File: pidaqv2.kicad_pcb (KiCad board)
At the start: 2 copper layers, 66 x 66 mm, 20 parts, among them J1 Raspberry_Pi_2_3, U1 INA2126E_250, U2 ADS114S08BIPBS, U3 ADS114S08BIPBS

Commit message: ads1261
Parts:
- removed C1, C4, C7, C8, C9: 0.1uF, Capacitor_SMD:C_0805_2012Metric_Pad1.15x1.40mm_HandSolder
- removed C2, C5: 330nF, Capacitor_SMD:C_0805_2012Metric_Pad1.15x1.40mm_HandSolder
- removed C3, C6: 1uF, Capacitor_SMD:C_0805_2012Metric_Pad1.15x1.40mm_HandSolder
- removed J1: Raspberry_Pi_2_3, Connector_PinHeader_2.54mm:PinHeader_2x20_P2.54mm_Vertical
- removed JAIN0: Screw_Terminal_01x10, TerminalBlock_TE-Connectivity:TerminalBlock_TE_1-282834-0_1x10_P2.54mm_Horizontal
- removed JAIN1: Screw_Terminal_01x12, TerminalBlock_TE-Connectivity:TerminalBlock_TE_1-282834-2_1x12_P2.54mm_Horizontal
- removed JLC1, JTC-1: Screw_Terminal_01x06, TerminalBlock_TE-Connectivity:TerminalBlock_TE_282834-6_1x06_P2.54mm_Horizontal
- removed MK1, MK2, MK3: MountingHole_Pad, MountingHole:MountingHole_2.7mm_M2.5_ISO14580_Pad
- removed U1: INA2126E_250, footprints:INA2126E&slash_250
- removed U2, U3: ADS114S08BIPBS, footprints:ADS114S08BIPBS
- added C101: 0.1uF, Capacitor_SMD:C_0603_1608Metric, F.Cu at (124.6, 97.3)
- added C102: 0.1uF, Capacitor_SMD:C_0603_1608Metric, F.Cu at (127.8, 96.3)
- added C201: 4.7nF C0G, Capacitor_SMD:C_0603_1608Metric, F.Cu at (137.3, 91.5)
- added C202: 1uF, Capacitor_SMD:C_0603_1608Metric, F.Cu at (134.6, 93.6)
- added C203: 10uF, Capacitor_SMD:C_0603_1608Metric, F.Cu at (135.4, 95.9)
- added C204: 1uF, Capacitor_SMD:C_0603_1608Metric, F.Cu at (148.3, 95.5)
- added C205: 1uF, Capacitor_SMD:C_0603_1608Metric, F.Cu at (145.1, 97.7)
- added C206: 10uF, Capacitor_SMD:C_0603_1608Metric, F.Cu at (134.6, 91.3)
- added C301: 4.7nF C0G, Capacitor_SMD:C_0603_1608Metric, F.Cu at (140.3, 119.9)
- added C302: 1uF, Capacitor_SMD:C_0603_1608Metric, F.Cu at (140.9, 117.0)
- added C303: 10uF, Capacitor_SMD:C_0603_1608Metric, F.Cu at (140.9, 115.1)
- added C304: 1uF, Capacitor_SMD:C_0603_1608Metric, F.Cu at (129.5, 114.0)
- added C305: 1uF, Capacitor_SMD:C_0603_1608Metric, F.Cu at (132.5, 111.6)
- added C306: 10uF, Capacitor_SMD:C_0603_1608Metric, F.Cu at (143.6, 118.9)
- added H101: MountingHole, MountingHole:MountingHole_3.2mm_M3_ISO7380, F.Cu at (172.7, 134.6)
- added H102: MountingHole, MountingHole:MountingHole_3.2mm_M3_ISO7380, F.Cu at (101.6, 134.6)
- added H103: MountingHole, MountingHole:MountingHole_3.2mm_M3_ISO7380, F.Cu at (172.7, 73.7)
- added H104: MountingHole, MountingHole:MountingHole_3.2mm_M3_ISO7380, F.Cu at (101.6, 73.7)
- added J101: Conn_02x04_Odd_Even, Connector_PinHeader_2.54mm:PinHeader_2x04_P2.54mm_Vertical, F.Cu at (165.1, 94.0)
- added J102: Conn_01x03, Connector_PinHeader_2.54mm:PinHeader_1x03_P2.54mm_Vertical, F.Cu at (162.6, 114.3)
- added J103: Screw_Terminal_01x10, TerminalBlock_Phoenix:TerminalBlock_Phoenix_MKDS-1,5-10-5.08_1x10_P5.08mm_Horizontal, F.Cu at (116.8, 81.3)
- added J104: Screw_Terminal_01x08, TerminalBlock_Phoenix:TerminalBlock_Phoenix_MPT-0,5-8-2.54_1x08_P2.54mm_Horizontal, F.Cu at (111.8, 129.5)
- added J105: Screw_Terminal_01x06, TerminalBlock_Phoenix:TerminalBlock_Phoenix_MKDS-3-6-5.08_1x06_P5.08mm_Horizontal, F.Cu at (111.8, 118.6)
- added J106: Screw_Terminal_01x08, TerminalBlock_Phoenix:TerminalBlock_Phoenix_MPT-0,5-8-2.54_1x08_P2.54mm_Horizontal, F.Cu at (134.6, 129.5)
- added J107: Conn_01x01_Female, Connector_PinHeader_2.54mm:PinHeader_1x01_P2.54mm_Vertical, F.Cu at (129.7, 88.8)
- added U101: INA2126E_250, footprints:INA2126E&slash_250, F.Cu at (124.8, 103.4)
- added U201: ADS1261BIRHBR, footprints:ADS1261BIRHBR, F.Cu at (142.0, 93.8)
- added U301: ADS1261BIRHBR, footprints:ADS1261BIRHBR, F.Cu at (134.6, 116.8)
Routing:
- net +3V3: track 56.3 -> 145.3 mm, vias 2 -> 3
- net TC-: track 0.00 -> 76.7 mm
- net +2.5V: track 51.8 -> 0.00 mm, vias 2 -> 0
- net /ADC_Module/A11: track 39.3 -> 0.00 mm
- net /sheet5F3BC562/A1: track 38.4 -> 0.00 mm
- net ~CS1: track 0.00 -> 37.6 mm
- net /ADC_Module/A10: track 37.1 -> 0.00 mm
- net /sheet5F3BC562/A0: track 35.6 -> 0.00 mm
- net /ADC_Module/A9: track 34.9 -> 0.00 mm
- net /ADC_Module/A8: track 32.8 -> 0.00 mm
- net /sheet5F3BC562/A2: track 32.1 -> 0.00 mm
- net /sheet5F3BC562/A5: track 31.5 -> 0.00 mm
- net /sheet5F3BC562/A4: track 31.3 -> 0.00 mm
- net /sheet5F3BC562/A3: track 31.1 -> 0.00 mm
- net /ADC0/AIN0: track 0.00 -> 30.0 mm
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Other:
- board size 66 x 66 mm -> 81.3 x 71.1 mm
- net class Default: clearance 0.1778 -> 0.2032; trace_width 0.1778 -> 0.2032
- rule pad_to_mask_clearance: 0.051 -> 0
- rule trace_clearance: 0.1778 -> 0.2032
- rule trace_min: 0.1778 -> 0.2032
- rule via_min_drill: 0.3 -> 0.381
- rule via_min_size: 0.3048 -> 0.3302
- board text added: "+3.3V"
- board text added: "+5V"
- board text added: "+EXC"
- board text added: "LC0+"
- board text added: "LC0-"
- board text added: "LC1+"
- board text added: "LC1-"
- board text added: "MISO"
- board text added: "MOSI"
- board text added: "PT0"
- board text added: "PT1"
- board text added: "PT2"
- board text added: "PT3"
- board text added: "PT4"
- board text added: "PT5"
- board text added: "PT6"
- board text added: "PT7"
- board text added: "PT8"
- board text added: "PT9"
- board text added: "Raspi mounted here"
- board text added: "SCLK"
- board text added: "TC0+"
- board text added: "TC0-"
- board text added: "TC1+"
- board text added: "TC1-"
- board text added: "TC2+"
- board text added: "TC2-"
- board text added: "TC3+"
- board text added: "TC3-"
- board text added: "TC4+"
- board text added: "TC4-"
- board text added: "TC5+"
- board text added: "TC5-"
- board text added: "TC6+"
- board text added: "TC6-"
- board text added: "TC7+"
- board text added: "TC7-"
- board text added: "UCLA Rocket Project DAQ 2020-2021"
- board text added: "~CS0"
- board text added: "~CS1"
- board text removed: "0"
- board text removed: "0+"
- board text removed: "0-"
- board text removed: "1"
- board text removed: "1+"
- board text removed: "1-"
- board text removed: "10"
- board text removed: "11"
- board text removed: "2"
- board text removed: "3"
- board text removed: "4"
- board text removed: "5"
- board text removed: "6"
- board text removed: "7"
- board text removed: "8"
- board text removed: "9"
- board text removed: "EXC"
- board text removed: "Load Cells"
- board text removed: "Thermocouple -'s"
- board text removed: "UCLA Rocket Project DAQ Module V1"
- board text removed: "V=2.5V"

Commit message: last highfreq
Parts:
- J107: value Conn_01x01_Female -> Conn_01x03_Male; footprint Connector_PinHeader_2.54mm:PinHeader_1x01_P2.54mm_Vertical -> Connector_PinHeader_2.54mm:PinHeader_1x03_P2.54mm_Vertical
- moved J107 20.1 mm to (109.7, 86.4), turned to 180 degrees
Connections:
- J104 pad 1: TC7 -> (no net)
- J107 pad 1: /ADC0/AIN- -> 2.5V
- U301 pad 25: TC7 -> (no net)
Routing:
- net 2.5V: track 25.1 -> 53.5 mm, vias 2 -> 3
- net TC7: track 27.2 -> 0.00 mm
- net (no net): track 0.00 -> 27.2 mm
- net /ADC0/AIN-: track 11.5 -> 34.2 mm
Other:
- net class Power added: clearance 0.2032, trace_width 0.508, via_dia 0.8, via_drill 0.4
- board text added: "2.5V"
- board text added: "AIN-"

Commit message: boi did i cut up that ground plane
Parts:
- removed C101, C102: 0.1uF, Capacitor_SMD:C_0603_1608Metric
- removed J106: Screw_Terminal_01x08, TerminalBlock_Phoenix:TerminalBlock_Phoenix_MPT-0,5-8-2.54_1x08_P2.54mm_Horizontal
- removed J107: Conn_01x03_Male, Connector_PinHeader_2.54mm:PinHeader_1x03_P2.54mm_Vertical
- removed U101: INA2126E_250, footprints:INA2126E&slash_250
- added A101: Arduino_UNO_R3, Module:Arduino_UNO_R3, F.Cu at (86.4, 71.1)
- added C401: 0.1uF, Capacitor_SMD:C_0805_2012Metric_Pad1.15x1.40mm_HandSolder, F.Cu at (120.2, 98.5)
- added C402: 10uF, Capacitor_SMD:C_0805_2012Metric_Pad1.15x1.40mm_HandSolder, F.Cu at (123.2, 98.5)
- added R201: 4.7K, Resistor_SMD:R_0805_2012Metric_Pad1.15x1.40mm_HandSolder, F.Cu at (81.6, 101.4)
- added R301: 4.7K, Resistor_SMD:R_0805_2012Metric_Pad1.15x1.40mm_HandSolder, F.Cu at (102.9, 85.4)
- added U401: AD8426ACPZ-R7, footprints:AD8426ACPZ-R7, F.Cu at (119.7, 93.2)
- C201, C202, C203, C204, C205, C206, C301, C302, C303, C304, C305, C306: footprint Capacitor_SMD:C_0603_1608Metric -> Capacitor_SMD:C_0805_2012Metric_Pad1.15x1.40mm_HandSolder
- J101: value Conn_02x04_Odd_Even -> Screw_Terminal_01x11; footprint Connector_PinHeader_2.54mm:PinHeader_2x04_P2.54mm_Vertical -> TerminalBlock_Phoenix:TerminalBlock_Phoenix_MKDS-3-11-5.08_1x11_P5.08mm_Horizontal
- J102: value Conn_01x03 -> Screw_Terminal_01x06; footprint Connector_PinHeader_2.54mm:PinHeader_1x03_P2.54mm_Vertical -> TerminalBlock_Phoenix:TerminalBlock_Phoenix_MKDS-1,5-6-5.08_1x06_P5.08mm_Horizontal
- J103: value Screw_Terminal_01x10 -> Conn_01x02_Male; footprint TerminalBlock_Phoenix:TerminalBlock_Phoenix_MKDS-1,5-10-5.08_1x10_P5.08mm_Horizontal -> Connector_PinHeader_2.54mm:PinHeader_1x02_P2.54mm_Vertical
- J105: value Screw_Terminal_01x06 -> Screw_Terminal_01x04; footprint TerminalBlock_Phoenix:TerminalBlock_Phoenix_MKDS-3-6-5.08_1x06_P5.08mm_Horizontal -> TerminalBlock_Phoenix:TerminalBlock_Phoenix_MPT-0,5-4-2.54_1x04_P2.54mm_Horizontal
- U201, U301: footprint footprints:ADS1261BIRHBR -> Package_DFN_QFN:Texas_S-PVQFN-N32_EP3.45x3.45mm
- moved H103 112.8 mm to (61.0, 58.4)
- moved H101 111.7 mm to (61.3, 143.1)
- moved J101 104.0 mm to (69.5, 134.9)
- moved H102 85.2 mm to (139.7, 58.4)
- moved H104 79.2 mm to (139.7, 143.1)
- moved C204 77.6 mm to (71.5, 105.7), turned to 180 degrees
- moved C205 69.5 mm to (75.7, 101.9), turned to 180 degrees
- moved J104 66.1 mm to (114.3, 63.5), turned to 180 degrees
- moved U201 65.2 mm to (78.2, 107.4), turned to 180 degrees
- moved C301 58.7 mm to (99.9, 77.3), turned to 270 degrees
- moved C306 58.4 mm to (96.3, 84.7), turned to 180 degrees
- moved J103 58.2 mm to (78.7, 125.2), turned to 90 degrees
- moved C302 57.2 mm to (96.3, 81.1), turned to 180 degrees
- moved C201 55.8 mm to (84.5, 109.8), turned to 90 degrees
- moved J105 52.7 mm to (134.6, 71.1), turned to 270 degrees
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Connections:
- net TC- renamed /ADC1/AINCOM
- C203 pad 1: 2.5V -> /ADC0/REF2.5V
- J101 pad 1: GND -> /ADC0/AIN9
- J101 pad 2: MOSI -> /ADC0/AIN8
- J101 pad 3: (no net) -> /ADC0/AIN7
- J101 pad 4: MISO -> /ADC0/AIN6
- J101 pad 5: ~CS0 -> /ADC0/AIN5
- J101 pad 6: SCLK -> /ADC0/AIN4
- J101 pad 7: ~CS1 -> /ADC0/AIN3
- J101 pad 8: GND -> /ADC0/AIN2
- J102 pad 1: +5V -> /amplifier/A+
- J102 pad 2: +3V3 -> /amplifier/A-
- J102 pad 3: GND -> /amplifier/B+
- J103 pad 1: /ADC0/AIN0 -> /ADC0/AINCOM
- J103 pad 2: /ADC0/AIN1 -> GND
- J104 pad 1: (no net) -> /ADC1/AIN3
- J104 pad 3: TC6 -> /ADC1/AIN2
- J104 pad 5: TC5 -> /ADC1/AIN1
- J104 pad 7: TC4 -> /ADC1/AIN0
- J105 pad 1: GND -> /ADC1/AIN4
- J105 pad 2: LC0- -> /ADC1/AIN5
- J105 pad 3: LC0+ -> /ADC1/AIN6
- J105 pad 4: LC1- -> /ADC1/AIN7
- U201 pad 1: /ADC0/AIN- -> /ADC0/AINCOM
- U201 pad 6: 2.5V -> /ADC0/REF2.5V
- U301 pad 23: LC1 -> /A
- U301 pad 24: LC0 -> /B
- U301 pad 25: (no net) -> /ADC1/AIN7
- U301 pad 26: TC6 -> /ADC1/AIN6
- U301 pad 27: TC5 -> /ADC1/AIN5
- U301 pad 28: TC4 -> /ADC1/AIN4
- U301 pad 29: TC3 -> /ADC1/AIN3
- U301 pad 30: TC2 -> /ADC1/AIN2
- U301 pad 31: TC1 -> /ADC1/AIN1
- U301 pad 32: TC0 -> /ADC1/AIN0
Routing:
- net /ADC0/REF2.5V: track 0.00 -> 64.6 mm, vias 0 -> 2
- net 2.5V: track 53.5 -> 0.00 mm, vias 3 -> 0
- net /amplifier/A-: track 0.00 -> 50.0 mm
- net /ADC1/REF2.5V: track 3.49 -> 45.2 mm, vias 0 -> 4
- net /ADC0/AIN1: track 24.7 -> 61.5 mm
- net /ADC0/AIN2: track 20.2 -> 56.8 mm
- net /ADC0/AIN0: track 30.0 -> 66.5 mm
- net /ADC0/AIN3: track 15.7 -> 52.1 mm
- net /ADC1/AINCOM: track 76.7 -> 41.1 mm
- net /ADC0/AIN4: track 12.9 -> 47.9 mm
- net /ADC0/AIN-: track 34.2 -> 0.00 mm
- net /ADC1/AIN4: track 0.00 -> 32.7 mm
- net /ADC0/AIN5: track 10.4 -> 42.8 mm
- net /ADC1/AIN6: track 0.00 -> 31.7 mm
- net /ADC1/AIN5: track 0.00 -> 31.2 mm
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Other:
- board size 81.3 x 71.1 mm -> 86.4 x 92.1 mm
- net class Default: clearance 0.2032 -> 0.1778; trace_width 0.2032 -> 0.1778
- rule trace_clearance: 0.2032 -> 0.1778
- rule trace_min: 0.2032 -> 0.1524
- board text removed: "+3.3V"
- board text removed: "+5V"
- board text removed: "+EXC"
- board text removed: "2.5V"
- board text removed: "AIN-"
- board text removed: "GND"
- board text removed: "LC0+"
- board text removed: "LC0-"
- board text removed: "LC1+"
- board text removed: "LC1-"
- board text removed: "MISO"
- board text removed: "MOSI"
- board text removed: "PT0"
- board text removed: "PT1"
- board text removed: "PT2"
- board text removed: "PT3"
- board text removed: "PT4"
- board text removed: "PT5"
- board text removed: "PT6"
- board text removed: "PT7"
- board text removed: "PT8"
- board text removed: "PT9"
- board text removed: "Raspi mounted here"
- board text removed: "SCLK"
- board text removed: "TC0+"
- board text removed: "TC0-"
- board text removed: "TC1+"
- board text removed: "TC1-"
- board text removed: "TC2+"
- board text removed: "TC2-"
- board text removed: "TC3+"
- board text removed: "TC3-"
- board text removed: "TC4+"
- board text removed: "TC4-"
- board text removed: "TC5+"
- board text removed: "TC5-"
- board text removed: "TC6+"
- board text removed: "TC6-"
- board text removed: "TC7+"
- board text removed: "TC7-"
- board text removed: "UCLA Rocket Project DAQ 2020-2021"
- board text removed: "~CS0"
- board text removed: "~CS1"

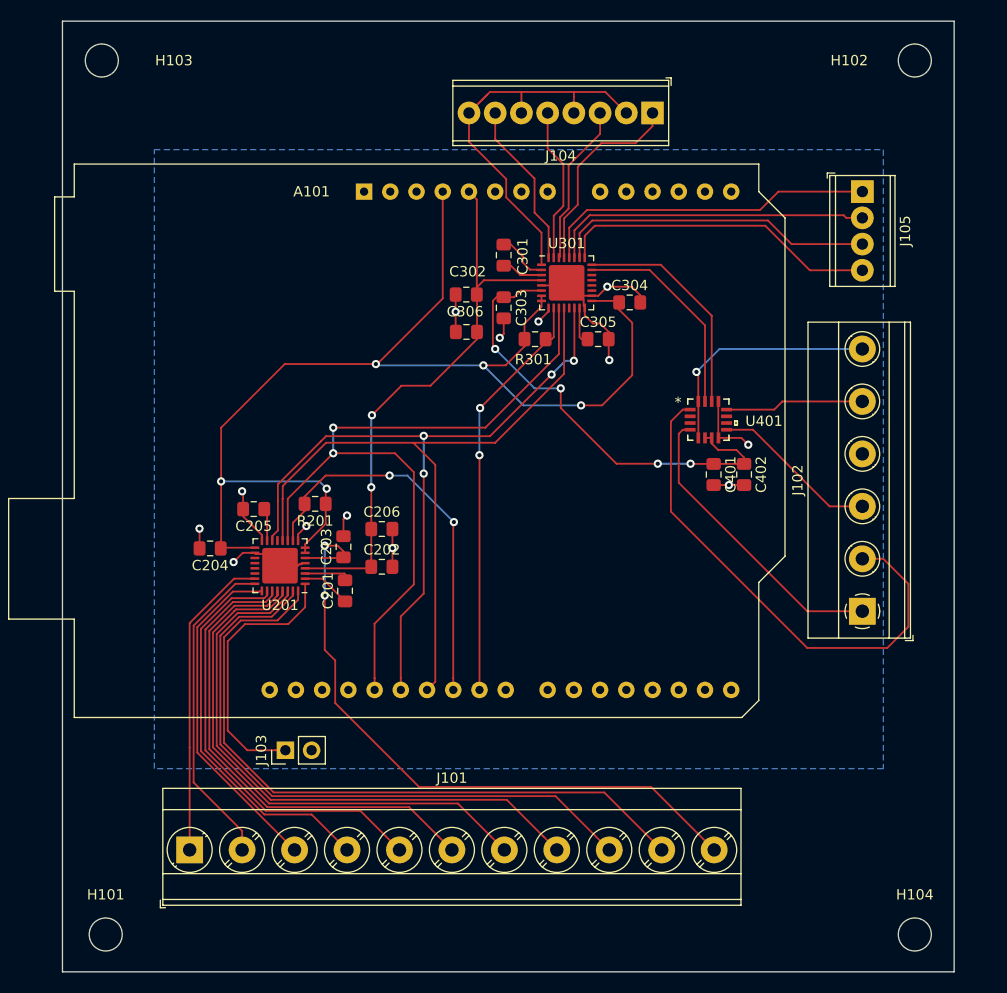
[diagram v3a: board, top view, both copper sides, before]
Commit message: add silkscreen labels
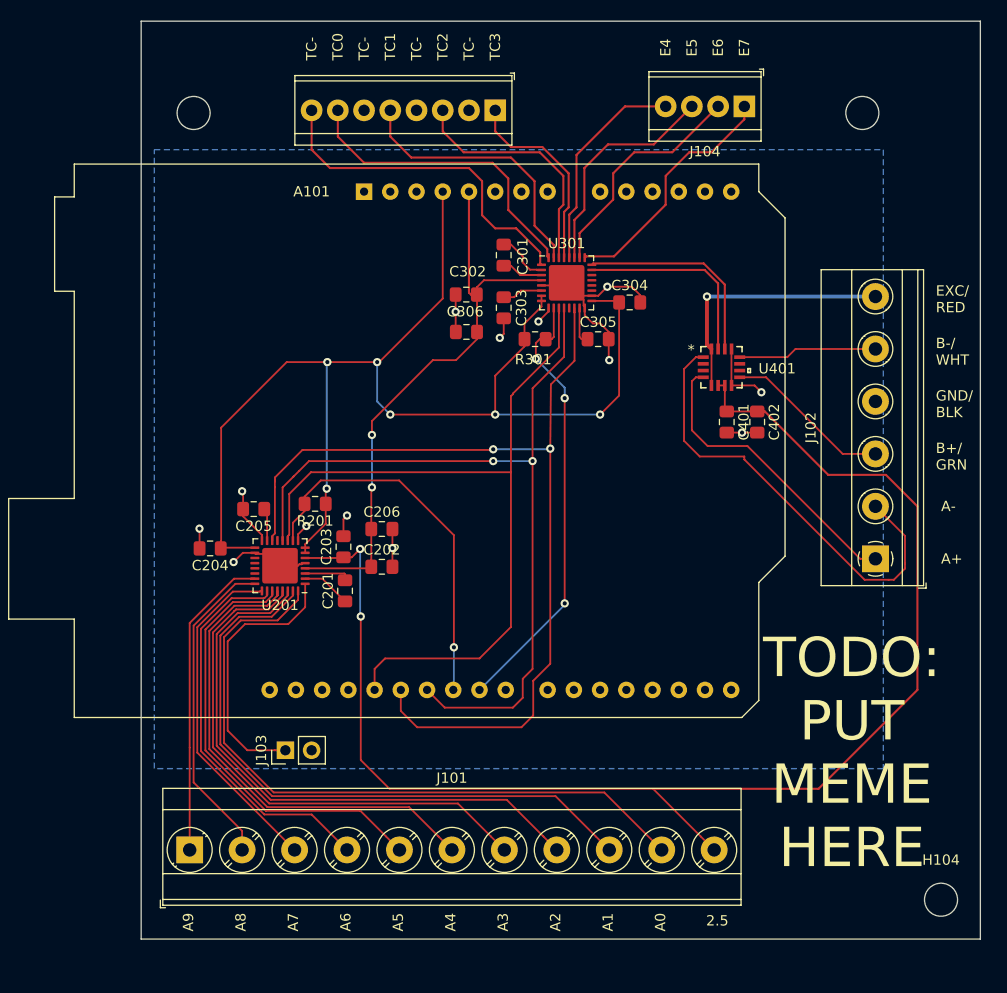
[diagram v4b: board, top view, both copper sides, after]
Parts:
- removed H101: MountingHole, MountingHole:MountingHole_3.2mm_M3_ISO7380
- J104: value Screw_Terminal_01x08 -> Screw_Terminal_01x04; footprint TerminalBlock_Phoenix:TerminalBlock_Phoenix_MPT-0,5-8-2.54_1x08_P2.54mm_Horizontal -> TerminalBlock_TE-Connectivity:TerminalBlock_TE_282834-4_1x04_P2.54mm_Horizontal
- J105: value Screw_Terminal_01x04 -> Screw_Terminal_01x08; footprint TerminalBlock_Phoenix:TerminalBlock_Phoenix_MPT-0,5-4-2.54_1x04_P2.54mm_Horizontal -> TerminalBlock_TE-Connectivity:TerminalBlock_TE_282834-8_1x08_P2.54mm_Horizontal
- moved J105 36.4 mm to (99.1, 63.2), turned to 180 degrees
- moved H103 10.2 mm to (69.8, 63.5)
- moved J104 8.91 mm to (123.2, 62.9)
- moved H102 7.18 mm to (134.6, 63.5)
- moved U401 5.24 mm to (121.0, 88.1)
- moved C401 5.24 mm to (121.5, 93.4)
- moved C402 5.24 mm to (124.4, 93.4)
- moved J102 5.24 mm to (135.9, 106.7)
- moved H104 4.22 mm to (142.2, 139.7)
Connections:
- C203 pad 1: /ADC0/REF2.5V -> 2.5V
- C401 pad 1: /ADC1/REF2.5V -> 2.5V
- C402 pad 1: /ADC1/REF2.5V -> 2.5V
- J101 pad 11: /ADC0/REF2.5V -> 2.5V
- J104 pad 1: /ADC1/AIN3 -> /ADC1/AIN7
- J104 pad 2: /ADC1/AINCOM -> /ADC1/AIN6
- J104 pad 3: /ADC1/AIN2 -> /ADC1/AIN5
- J104 pad 4: /ADC1/AINCOM -> /ADC1/AIN4
- J105 pad 1: /ADC1/AIN4 -> /ADC1/AIN3
- J105 pad 2: /ADC1/AIN5 -> /ADC1/AINCOM
- J105 pad 3: /ADC1/AIN6 -> /ADC1/AIN2
- J105 pad 4: /ADC1/AIN7 -> /ADC1/AINCOM
- U201 pad 6: /ADC0/REF2.5V -> 2.5V
- U401 pad 6: /ADC1/REF2.5V -> 2.5V
- U401 pad 7: /ADC1/REF2.5V -> 2.5V
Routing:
- net 2.5V: track 0.00 -> 138.1 mm, vias 0 -> 2
- net /ADC0/REF2.5V: track 64.6 -> 0.00 mm, vias 2 -> 0
- net /ADC1/REF2.5V: track 45.2 -> 3.92 mm, vias 4 -> 0
- net MISO: track 69.8 -> 91.1 mm, vias 4 -> 2
- net /ADC1/AIN0: track 16.2 -> 30.0 mm
- net /ADC1/AIN4: track 32.7 -> 20.8 mm
- net MOSI: track 68.6 -> 80.3 mm, vias 0 -> 2
- net /ADC1/AIN1: track 15.0 -> 26.5 mm
- net /ADC1/AIN5: track 31.2 -> 22.0 mm
- net /ADC1/AIN6: track 31.7 -> 22.8 mm
- net /ADC1/AIN2: track 15.7 -> 23.6 mm
- net /ADC1/AINCOM: track 41.1 -> 33.3 mm
- net /ADC1/AIN7: track 31.2 -> 23.9 mm
- net +3V3: track 118.0 -> 125.3 mm, vias 5 -> 6
- net /amplifier/A-: track 50.0 -> 44.1 mm
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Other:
- board size 86.4 x 92.1 mm -> 81.3 x 88.9 mm
- board text added: "2.5"
- board text added: "A+"
- board text added: "A-"
- board text added: "A0"
- board text added: "A1"
- board text added: "A2"
- board text added: "A3"
- board text added: "A4"
- board text added: "A5"
- board text added: "A6"
- board text added: "A7"
- board text added: "A8"
- board text added: "A9"
- board text added: "B+/ GRN"
- board text added: "B-/ WHT"
- board text added: "E4"
- board text added: "E5"
- board text added: "E6"
- board text added: "E7"
- board text added: "EXC/ RED"
- board text added: "GND/ BLK"
- board text added: "TC-"
- board text added: "TC0"
- board text added: "TC1"
- board text added: "TC2"
- board text added: "TC3"
- board text added: "TODO: PUT MEME HERE"
